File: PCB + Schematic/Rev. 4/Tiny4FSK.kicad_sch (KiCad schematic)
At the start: 90 parts, among them IC1 SI4063, J1 SWD, J10 USB, J2 GPIO, J3 USBC, J4 USB, J5 I2C, J6 Power, J7 SPI, J8 USB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

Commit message: USB Breakout
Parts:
- removed C1, C2, C29, C31: 100 nF, Capacitor_SMD:C_0805_2012Metric_Pad1.18x1.45mm_HandSolder, symbol Device:C_Small
- removed C22, C23: 1uF, Capacitor_SMD:C_0805_2012Metric_Pad1.18x1.45mm_HandSolder, symbol Device:C_Small
- removed C30, C7: 4.5 nF, Capacitor_SMD:C_0805_2012Metric_Pad1.18x1.45mm_HandSolder, symbol Device:C_Small
- removed FB1, FB2: BLM18AG121SN1D, Resistor_SMD:R_0603_1608Metric_Pad0.98x0.95mm_HandSolder, symbol Device:FerriteBead_Small
- removed J10, J8: USB, Connector_PinHeader_2.54mm:PinHeader_1x04_P2.54mm_Vertical, symbol Connector_Generic:Conn_01x04
- removed J3, J9: USBC, Connector_USB:USB_C_Receptacle_GCT_USB4105-xx-A_16P_TopMnt_Horizontal, symbol Connector:USB_C_Receptacle_USB2.0
- removed R16, R3: 1M, Resistor_SMD:R_0805_2012Metric_Pad1.20x1.40mm_HandSolder, symbol Device:R_Small_US
- removed R17, R18, R5, R7: 5k1, Resistor_SMD:R_0805_2012Metric_Pad1.20x1.40mm_HandSolder, symbol Device:R_Small_US
- removed U8: Linear Step-Down, LDO:MCP1700, symbol Regulator_Linear:MCP1700x-330xxTT
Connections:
- no-connect marks 32 -> 28
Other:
- note removed: "USB Step-Down Converter 5v -> 3.3v"
- moved on the sheet: C11, C23, D3, JP1, JP2, R13, R14, R15, SW2, U5

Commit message: USB Prog, updates
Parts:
- U5: footprint Oscillator_TCXO:ATXK-H11-E-32.768KHZ-E50-T3 -> Oscillator_TCXO:KDS-1XZA032768AD19
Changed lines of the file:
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@@
 			)
 		)
-		(property "Footprint" "Oscillator_TCXO:ATXK-H11-E-32.768KHZ-E50-T3"
+		(property "Footprint" "Oscillator_TCXO:KDS-1XZA032768AD19"
 			(at 247.65 118.11 0)
 			(effects

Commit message: 0402s for JLCPCB capabilities
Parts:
- C22, C27: footprint Capacitor_SMD:C_0201_0603Metric_Pad0.64x0.40mm_HandSolder -> Capacitor_SMD:C_0402_1005Metric_Pad0.74x0.62mm_HandSolder
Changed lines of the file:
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@@
 			)
 		)
-		(property "Footprint" "Capacitor_SMD:C_0201_0603Metric_Pad0.64x0.40mm_HandSolder"
+		(property "Footprint" "Capacitor_SMD:C_0402_1005Metric_Pad0.74x0.62mm_HandSolder"
 			(at 59.69 40.64 0)
 			(effects
@@
 			)
 		)
-		(property "Footprint" "Capacitor_SMD:C_0201_0603Metric_Pad0.64x0.40mm_HandSolder"
+		(property "Footprint" "Capacitor_SMD:C_0402_1005Metric_Pad0.74x0.62mm_HandSolder"
 			(at 44.45 40.64 0)
 			(effects

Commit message: Finish USB breakout
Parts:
- removed BT2: AAA, BatteryExtended:BAT_BK-82, symbol Device:Battery_Cell
- removed C23: 1uF, Capacitor_SMD:C_0805_2012Metric_Pad1.18x1.45mm_HandSolder, symbol Device:C_Small
- removed JP2: Source, Jumper:SolderJumper-3_P1.3mm_Open_Pad1.0x1.5mm_NumberLabels, symbol Jumper:Jumper_3_Open
- added BT1: Battery_Cell, BatteryExtended:BAT_53, symbol Device:Battery_Cell
- C19: LCSC (none) -> C5186894
- C2: value 10uF -> 100 nF
- C22: LCSC (none) -> C5447805
- C4, C9: value 100nF -> 10 uF
- C5: value 100nF -> 100 nF
- R11: value 900k -> 180k
- R12: value 5M -> 1M
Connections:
- net BOOST is gone; now on net +3.3V: C15.1, C16.1, R12.1, U2.2 (VOUT)
- net +BATT: now also BT1.1 (+)
- net Earth: now also BT1.2 (-)
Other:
- note added: "SAMD21G18A MCU + Voltmeter"
- note removed: "SAMD21G18A MCU + Voltmeter + USB"

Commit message: Make DRC happy
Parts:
- AE1: footprint RF_Antenna_Extended:ANT_1575AT_JOT -> RF_Antenna_Extended:GPS1003
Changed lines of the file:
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@@
 			)
 		)
-		(property "Footprint" "RF_Antenna_Extended:ANT_1575AT_JOT"
+		(property "Footprint" "RF_Antenna_Extended:GPS1003"
 			(at 72.39 66.04 0)
 			(effects

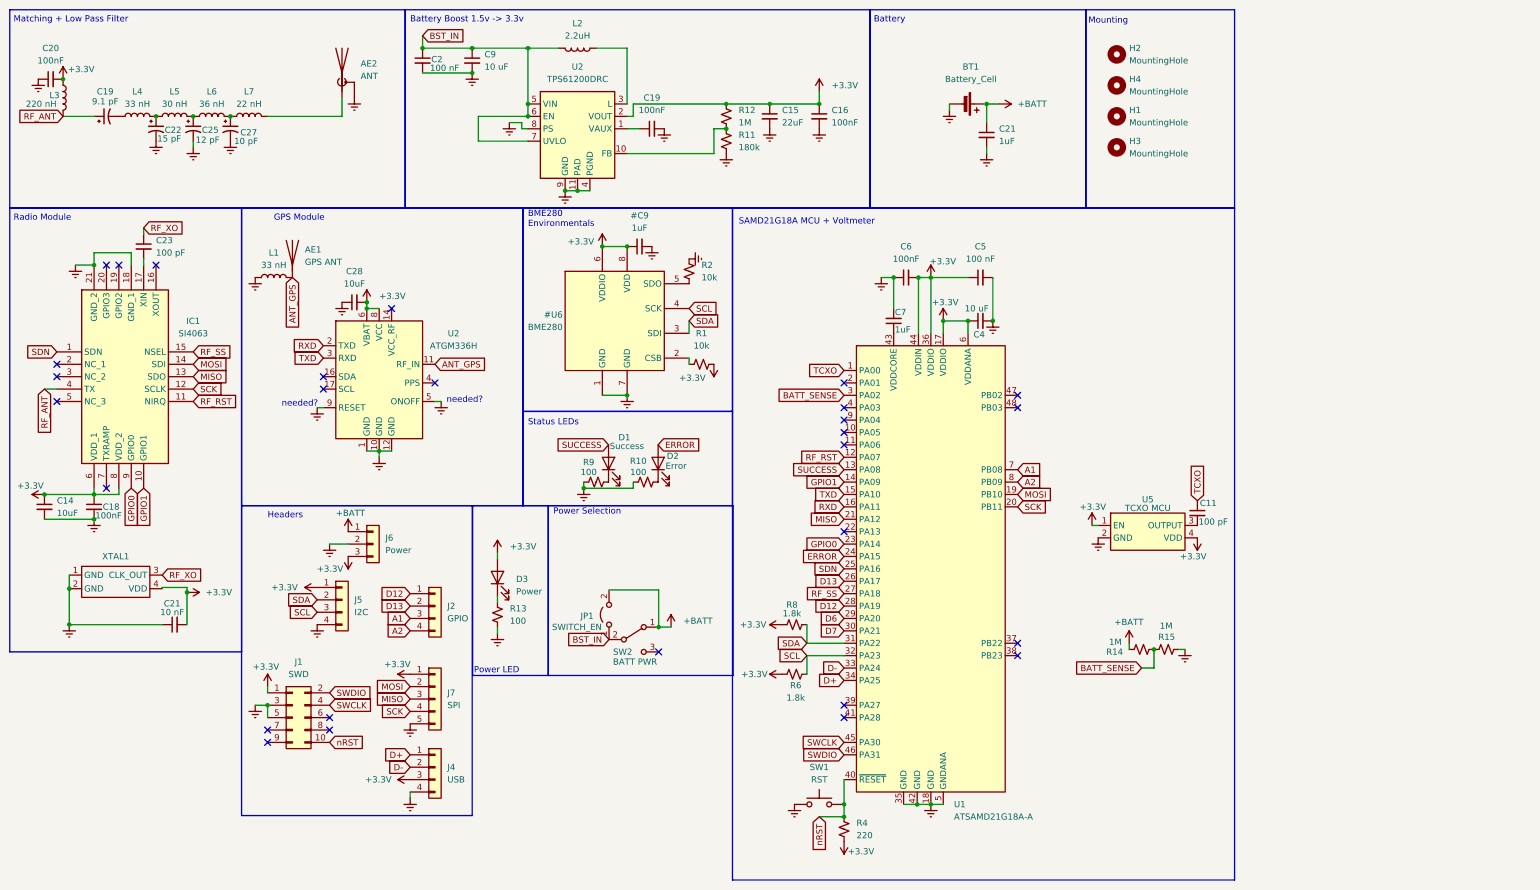
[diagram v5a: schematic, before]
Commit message: JLCPCB part numbering, PCB updates
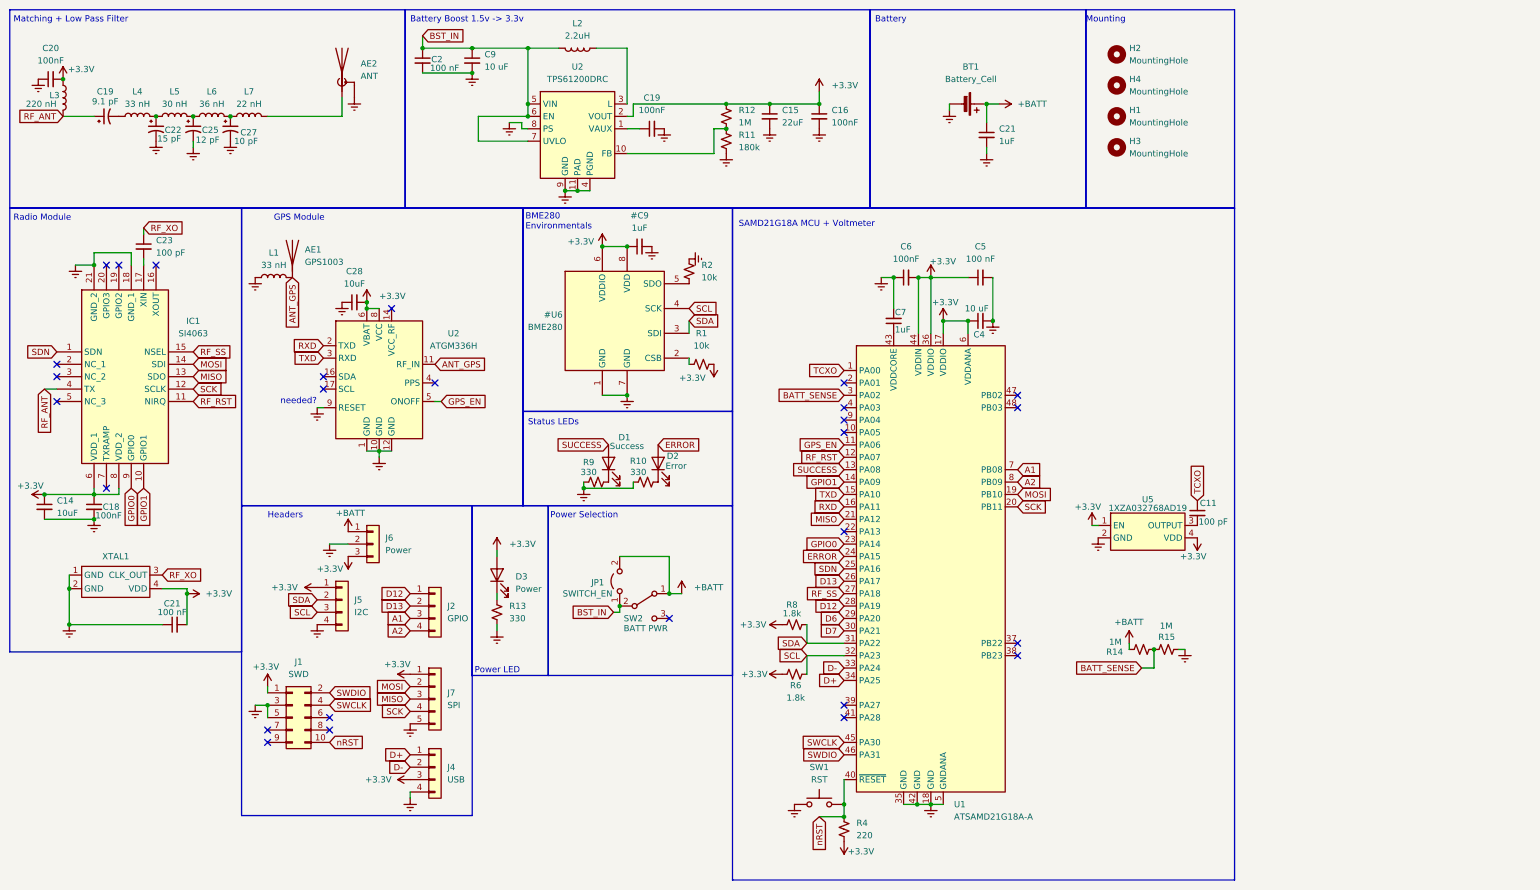
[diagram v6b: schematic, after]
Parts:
- #C9, C21, C7: footprint Capacitor_SMD:C_0805_2012Metric_Pad1.18x1.45mm_HandSolder -> Capacitor_SMD:C_0402_1005Metric_Pad0.74x0.62mm_HandSolder; LCSC (none) -> C52923
- #U6: LCSC (none) -> C92489
- AE1: value GPS ANT -> GPS1003; LCSC (none) -> C239243
- C11, C23: LCSC (none) -> C5186766
- C14, C28, C4, C9: footprint Capacitor_SMD:C_0805_2012Metric_Pad1.18x1.45mm_HandSolder -> Capacitor_SMD:C_0603_1608Metric_Pad1.08x0.95mm_HandSolder; LCSC (none) -> C19702
- C16, C18, C19, C2, C5, C6: footprint Capacitor_SMD:C_0805_2012Metric_Pad1.18x1.45mm_HandSolder -> Capacitor_SMD:C_0402_1005Metric_Pad0.74x0.62mm_HandSolder; LCSC (none) -> C1525
- C20: footprint Capacitor_SMD:C_0603_1608Metric_Pad1.08x0.95mm_HandSolder -> Capacitor_SMD:C_0402_1005Metric_Pad0.74x0.62mm_HandSolder; LCSC (none) -> C1525
- C21: value 10 nF -> 100 nF; footprint Capacitor_SMD:C_0805_2012Metric_Pad1.18x1.45mm_HandSolder -> Capacitor_SMD:C_0402_1005Metric_Pad0.74x0.62mm_HandSolder; LCSC (none) -> C1525
- C25: LCSC (none) -> C1547
- D1: LCSC (none) -> C2297
- D2: LCSC (none) -> C84256
- L6: LCSC (none) -> C408700
- R1, R2: LCSC (none) -> C2961403
- R10, R13, R9: value 100 -> 330; footprint Resistor_SMD:R_0805_2012Metric_Pad1.20x1.40mm_HandSolder -> Resistor_SMD:R_0603_1608Metric_Pad0.98x0.95mm_HandSolder
- R11: LCSC (none) -> C160534
- R12, R14, R15: LCSC (none) -> C313849
- R4: footprint Resistor_SMD:R_0805_2012Metric_Pad1.20x1.40mm_HandSolder -> Resistor_SMD:R_0402_1005Metric_Pad0.72x0.64mm_HandSolder; LCSC (none) -> C100308
- R6, R8: footprint Resistor_SMD:R_0805_2012Metric_Pad1.20x1.40mm_HandSolder -> Resistor_SMD:R_0603_1608Metric_Pad0.98x0.95mm_HandSolder; LCSC (none) -> C100820
- SW1: footprint Button_Switch_SMD:SW_Tactile_SPST_NO_Straight_CK_PTS636Sx25SMTRLFS -> Button_Switch_SMD:SW_SPST_CK_RS282G05A3
- SW2: footprint SlideSwitch:WS-SLSU_6p7x2p7_WRE -> Button_Switch_SMD:SW_SPDT_PCM12
- U1: LCSC (none) -> C78624
- U2: LCSC (none) -> C140320
- U2: LCSC (none) -> C5117921
- U5: value TCXO MCU -> 1XZA032768AD19; LCSC (none) -> C213398
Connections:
- net Earth: no longer U2.5 (ONOFF)
- net GPS_EN: now reaches U1.11 (PA06)
- net GPS_EN: now also U2.5 (ONOFF)
- no-connect marks 28 -> 27
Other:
- moved on the sheet: D3, JP1, R13, SW2

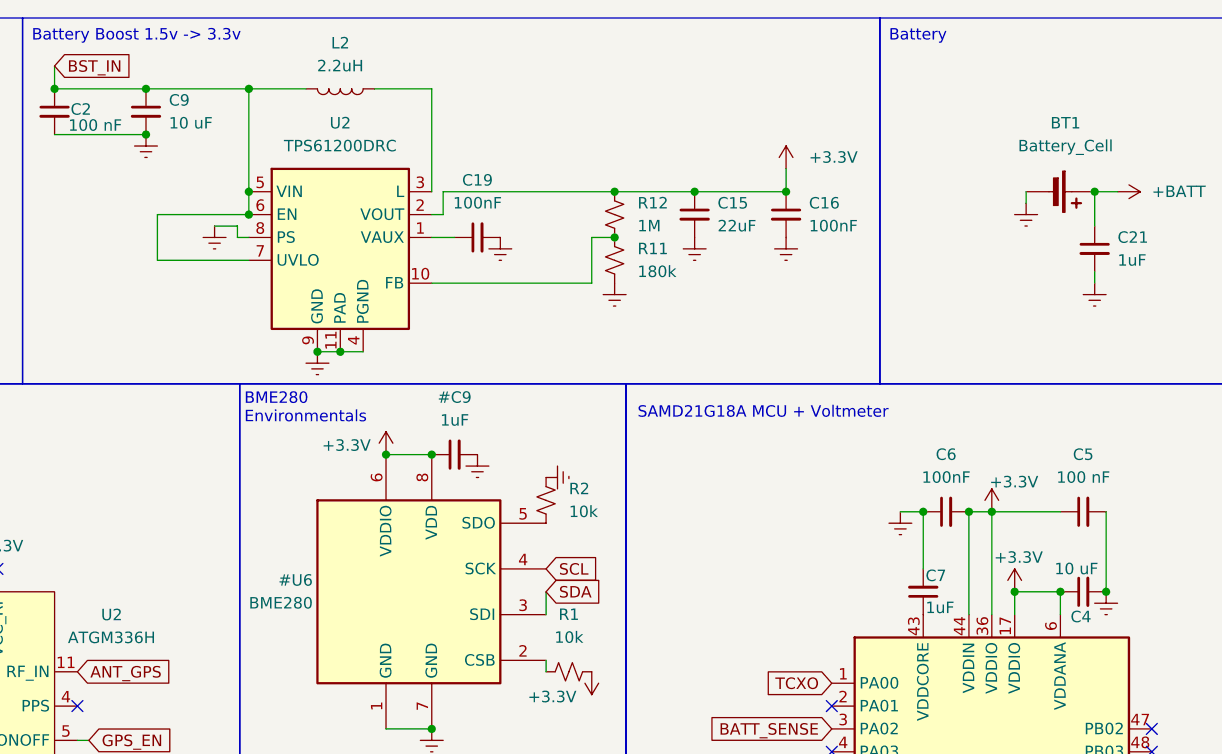
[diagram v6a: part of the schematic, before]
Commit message: New cheaper parts
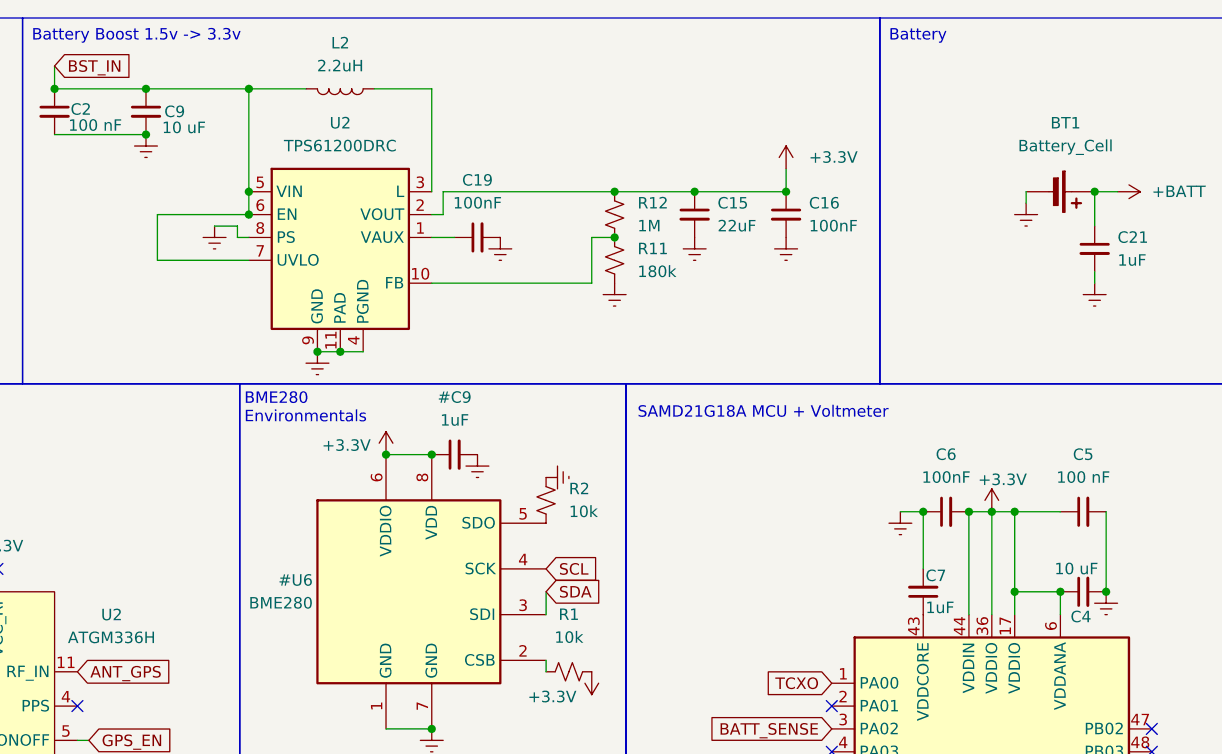
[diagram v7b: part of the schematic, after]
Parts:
- C11, C23: footprint Capacitor_SMD:C_0805_2012Metric_Pad1.18x1.45mm_HandSolder -> Capacitor_SMD:C_0402_1005Metric_Pad0.74x0.62mm_HandSolder; LCSC C5186766 -> C1546
- L2: LCSC (none) -> C2844756
- L5: LCSC (none) -> C330865
- R1, R2: footprint Resistor_SMD:R_0805_2012Metric_Pad1.20x1.40mm_HandSolder -> Resistor_SMD:R_0402_1005Metric_Pad0.72x0.64mm_HandSolder; LCSC C2961403 -> C25744
- R11: footprint Resistor_SMD:R_0805_2012Metric_Pad1.20x1.40mm_HandSolder -> Resistor_SMD:R_0402_1005Metric_Pad0.72x0.64mm_HandSolder; LCSC C160534 -> C100276
- R12, R14, R15: footprint Resistor_SMD:R_0805_2012Metric_Pad1.20x1.40mm_HandSolder -> Resistor_SMD:R_0402_1005Metric_Pad0.72x0.64mm_HandSolder; LCSC C313849 -> C26083
- R4: LCSC C100308 -> C25091
- R6, R8: LCSC C100820 -> C4177
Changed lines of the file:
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@@
 	)
 	(junction
-		(at 205.74 80.01)
-		(diameter 0)
-		(color 0 0 0 0)
-	)
-	(junction
 		(at 31.75 68.58)
 		(diameter 0)
@@
 	)
 	(junction
+		(at 205.74 71.12)
+		(diameter 0)
+		(color 0 0 0 0)
+	)
+	(junction
 		(at 26.67 142.24)
 		(diameter 0)
@@
 	)
 	(junction
+		(at 205.74 80.01)
+		(diameter 0)
+		(color 0 0 0 0)
+	)
+	(junction
 		(at 52.07 38.1)
 		(diameter 0)
@@
 	(wire
 		(pts
+			(xy 205.74 71.12) (xy 205.74 80.01)
+		)
+		(stroke
+			(width 0)
+			(type default)
+		)
+	)
+	(wire
+		(pts
 			(xy 119.38 39.37) (xy 119.38 40.64)
 		)
@@
 	(wire
 		(pts
+			(xy 205.74 71.12) (xy 210.82 71.12)
+		)
+		(stroke
+			(width 0)
+			(type default)
+		)
+	)
+	(wire
+		(pts
 			(xy 21.59 93.98) (xy 24.13 93.98)
 		)
@@
 	(wire
 		(pts
-			(xy 203.2 71.12) (xy 210.82 71.12)
+			(xy 203.2 71.12) (xy 205.74 71.12)
 		)
 		(stroke
@@
 			)
 		)
-		(property "LCSC" "C100820"
+		(property "LCSC" "C4177"
 			(at 175.26 142.24 90)
 			(effects
@@
 			)
 		)
+		(property "LCSC" "C2844756"
+			(at 130.81 24.13 90)
+			(effects
+				(font
+					(size 1.27 1.27)
+				)
+				(hide yes)
+			)
+		)
 		(pin "1"
 		)
@@
 			)
 		)
-		(property "Footprint" "Resistor_SMD:R_0805_2012Metric_Pad1.20x1.40mm_HandSolder"
+		(property "Footprint" "Resistor_SMD:R_0402_1005Metric_Pad0.72x0.64mm_HandSolder"
 			(at 251.46 147.32 0)
 			(effects
@@
 			)
 		)
-		(property "LCSC" "C313849"
+		(property "LCSC" "C26083"
 			(at 251.46 147.32 90)
 			(effects
@@
 			)
 		)
-		(property "Footprint" "Resistor_SMD:R_0805_2012Metric_Pad1.20x1.40mm_HandSolder"
+		(property "Footprint" "Resistor_SMD:R_0402_1005Metric_Pad0.72x0.64mm_HandSolder"
 			(at 161.29 38.1 0)
 			(effects
@@
 			)
 		)
-		(property "LCSC" "C313849"
+		(property "LCSC" "C26083"
 			(at 161.29 38.1 0)
 			(effects
@@
 			)
 		)
-		(property "Footprint" "Resistor_SMD:R_0805_2012Metric_Pad1.20x1.40mm_HandSolder"
+		(property "Footprint" "Resistor_SMD:R_0402_1005Metric_Pad0.72x0.64mm_HandSolder"
 			(at 161.29 43.18 0)
 			(effects
@@
 			)
 		)
-		(property "LCSC" "C160534"
+		(property "LCSC" "C100276"
 			(at 161.29 43.18 0)
 			(effects
@@
 			)
 		)
-		(property "LCSC" "C100820"
+		(property "LCSC" "C4177"
 			(at 175.26 152.4 90)
 			(effects
@@
 		)
 		(property "Value" "+3.3V"
-			(at 202.946 67.818 0)
+			(at 201.676 67.564 0)
 			(effects
 				(font
@@
 			)
 		)
-		(property "Footprint" "Resistor_SMD:R_0805_2012Metric_Pad1.20x1.40mm_HandSolder"
+		(property "Footprint" "Resistor_SMD:R_0402_1005Metric_Pad0.72x0.64mm_HandSolder"
 			(at 156.21 88.9 0)
 			(effects
@@
 			)
 		)
-		(property "LCSC" "C2961403"
+		(property "LCSC" "C25744"
 			(at 156.21 88.9 90)
 			(effects
@@
 			)
 		)
-		(property "Footprint" "Capacitor_SMD:C_0805_2012Metric_Pad1.18x1.45mm_HandSolder"
+		(property "Footprint" "Capacitor_SMD:C_0402_1005Metric_Pad0.74x0.62mm_HandSolder"
 			(at 41.91 64.77 0)
 			(effects
@@
 			)
 		)
-		(property "LCSC" "C5186766"
+		(property "LCSC" "C1546"
 			(at 41.91 64.77 0)
 			(effects
@@
 			)
 		)
-		(property "Footprint" "Resistor_SMD:R_0805_2012Metric_Pad1.20x1.40mm_HandSolder"
+		(property "Footprint" "Resistor_SMD:R_0402_1005Metric_Pad0.72x0.64mm_HandSolder"
 			(at 246.38 147.32 0)
 			(effects
@@
 			)
 		)
-		(property "LCSC" "C313849"
+		(property "LCSC" "C26083 "
 			(at 246.38 147.32 90)
 			(effects
@@
 		(on_board yes)
 		(dnp no)
-		(fields_autoplaced yes)
 		(property "Reference" "C9"
-			(at 111.76 25.4062 0)
+			(at 111.252 26.6762 0)
 			(effects
 				(font
@@
 		)
 		(property "Value" "10 uF"
-			(at 111.76 27.9462 0)
+			(at 110.998 28.4542 0)
 			(effects
 				(font
@@
 			)
 		)
-		(property "Footprint" "Capacitor_SMD:C_0805_2012Metric_Pad1.18x1.45mm_HandSolder"
+		(property "Footprint" "Capacitor_SMD:C_0402_1005Metric_Pad0.74x0.62mm_HandSolder"
 			(at 257.81 119.38 0)
 			(effects
@@
 			)
 		)
-		(property "LCSC" "C5186766"
+		(property "LCSC" "C1546"
 			(at 257.81 119.38 0)
 			(effects
@@
 			)
 		)
-		(pin "1"
-		)
-		(pin "2"
-		)
-		(instances
-			(project "Tiny4FSK"
-				(path "/afd8b0bc-328a-481f-8ddf-c1252dc3b440"
-					(reference "L5")
-					(unit 1)
-				)
-			)
-		)
-	)
-	(symbol
-		(lib_name "+3.3V_3")
-		(lib_id "power:+3.3V")
-		(at 205.74 80.01 0)
-		(unit 1)
-		(exclude_from_sim no)
-		(in_bom yes)
-		(on_board yes)
-		(dnp no)
-		(property "Reference" "#PWR013"
-			(at 205.74 83.82 0)
-			(effects
-				(font
-					(size 1.27 1.27)
-				)
-				(hide yes)
-			)
-		)
-		(property "Value" "+3.3V"
-			(at 203.454 76.2 0)
-			(effects
-				(font
-					(size 1.27 1.27)
-				)
-				(justify left)
-			)
-		)
-		(property "Footprint" ""
-			(at 205.74 80.01 0)
-			(effects
-				(font
-					(size 1.27 1.27)
-				)
-				(hide yes)
-			)
-		)
-		(property "Datasheet" ""
-			(at 205.74 80.01 0)
-			(effects
-				(font
-					(size 1.27 1.27)
-				)
-				(hide yes)
-			)
-		)
-		(property "Description" ""
-			(at 205.74 80.01 0)
+		(property "LCSC" "C330865"
+			(at 48.26 38.1 90)
 			(effects
 				(font
@@
 		(pin "1"
 		)
+		(pin "2"
+		)
 		(instances
-			(project "littleLoRa"
-				(path "/a5a889c1-410f-46fe-abfd-162a711bc057"
-					(reference "#PWR013")
-					(unit 1)
-				)
-			)
 			(project "Tiny4FSK"
 				(path "/afd8b0bc-328a-481f-8ddf-c1252dc3b440"
-					(reference "#PWR045")
+					(reference "L5")
 					(unit 1)
 				)
@@
 		(on_board yes)
 		(dnp no)
-		(fields_autoplaced yes)
 		(property "Reference" "C6"
 			(at 198.1263 64.77 90)
@@
 			)
 		)
-		(property "LCSC" "C100308"
+		(property "LCSC" "C25091"
 			(at 185.42 184.15 0)
 			(effects
@@
 			)
 		)
-		(property "Footprint" "Resistor_SMD:R_0805_2012Metric_Pad1.20x1.40mm_HandSolder"
+		(property "Footprint" "Resistor_SMD:R_0402_1005Metric_Pad0.72x0.64mm_HandSolder"
 			(at 153.67 69.85 0)
 			(effects
@@
 			)
 		)
-		(property "LCSC" "C2961403"
+		(property "LCSC" "C25744"
 			(at 153.67 69.85 0)
 			(effects

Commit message: More cheaper components (even more!)
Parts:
- C15: footprint Capacitor_SMD:C_0805_2012Metric_Pad1.18x1.45mm_HandSolder -> Capacitor_SMD:C_0603_1608Metric_Pad1.08x0.95mm_HandSolder; LCSC (none) -> C59461
- C19: LCSC C5186894 -> C161337
- C22: LCSC C5447805 -> C1548
- C27: LCSC (none) -> C32949
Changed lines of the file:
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@@
 			)
 		)
+		(property "LCSC" "C32949"
+			(at 59.69 40.64 0)
+			(effects
+				(font
+					(size 1.27 1.27)
+				)
+				(hide yes)
+			)
+		)
 		(pin "1"
 		)
@@
 			)
 		)
-		(property "Footprint" "Capacitor_SMD:C_0805_2012Metric_Pad1.18x1.45mm_HandSolder"
+		(property "Footprint" "Capacitor_SMD:C_0603_1608Metric_Pad1.08x0.95mm_HandSolder"
 			(at 170.18 38.1 0)
 			(effects
@@
 			)
 		)
+		(property "LCSC" "C59461"
+			(at 170.18 38.1 0)
+			(effects
+				(font
+					(size 1.27 1.27)
+				)
+				(hide yes)
+			)
+		)
 		(pin "1"
 		)
@@
 			)
 		)
-		(property "LCSC" "C5447805"
+		(property "LCSC" "C1548"
 			(at 44.45 40.64 0)
 			(effects
@@
 			)
 		)
-		(property "LCSC" "C5186894"
+		(property "LCSC" "C161337"
 			(at 34.29 38.1 90)
 			(effects
